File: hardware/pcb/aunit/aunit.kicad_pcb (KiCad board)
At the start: 2 copper layers, 62.2 x 21.6 mm, 48 parts, among them J1 BUS, J2 Input A, J3 Input B, J4 Control, J5 Flags, J6 Power, U1 74HC283, U2 74HC283, U3 74HC86, U4 74HC86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

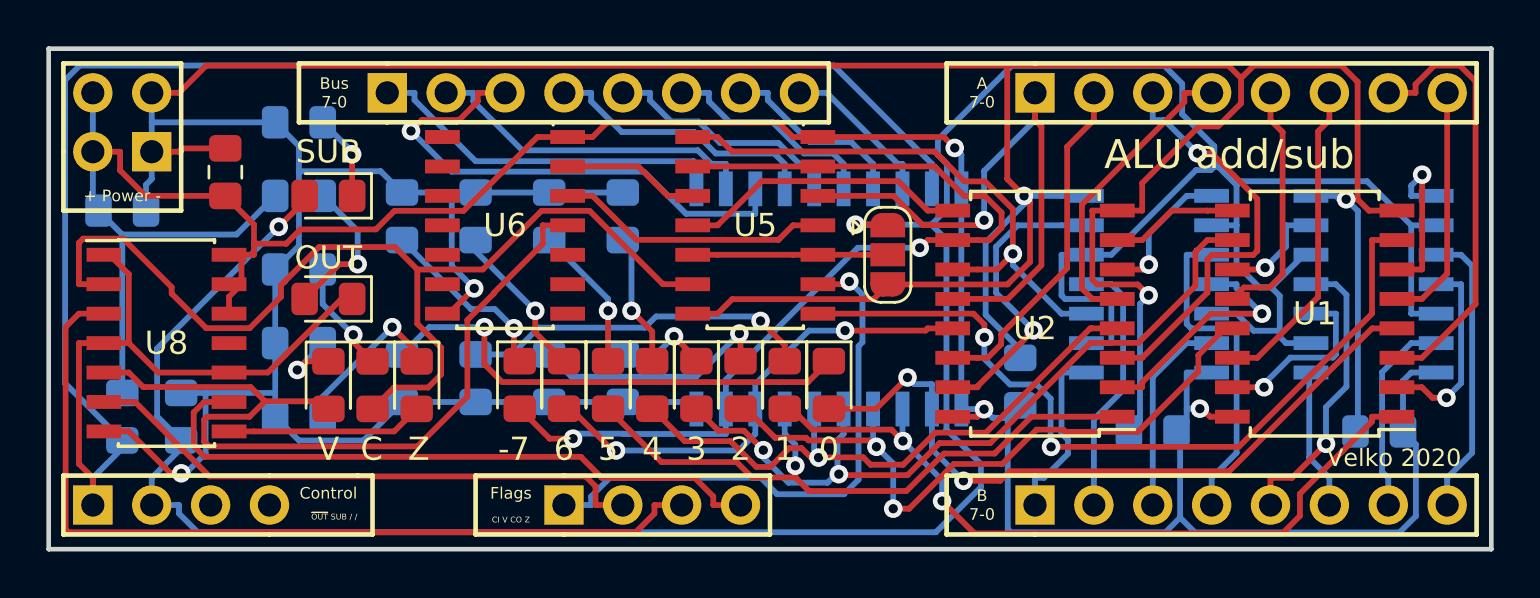
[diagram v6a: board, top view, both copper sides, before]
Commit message: Re-connect unused gate inputs, move input capacitor
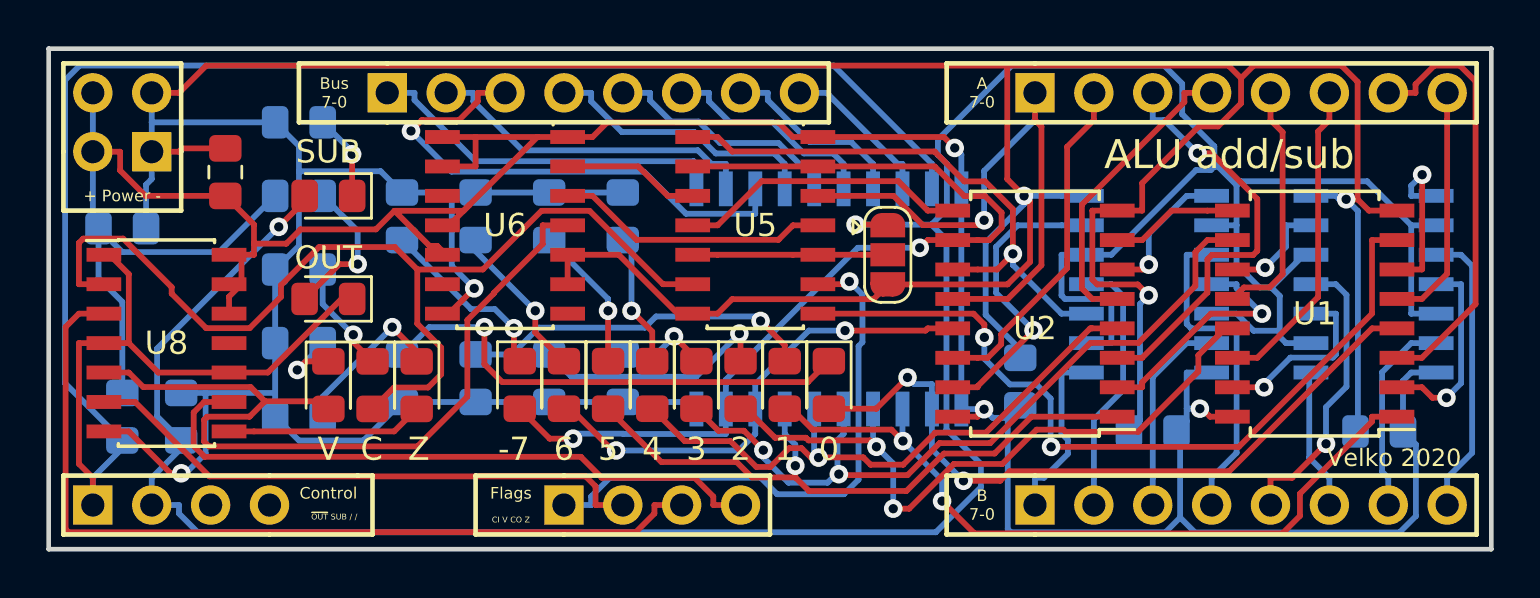
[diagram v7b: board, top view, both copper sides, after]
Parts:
- moved C1 0.76 mm to (38.1, 43.9)
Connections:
- U6 pad 1: Net-(U6-Pad1) -> VCC
- U6 pad 10: Net-(U6-Pad10) -> GND
- U6 pad 2: Net-(U6-Pad2) -> VCC
- U6 pad 4: Net-(U6-Pad4) -> VCC
- U6 pad 5: Net-(U6-Pad5) -> VCC
- U6 pad 9: Net-(U6-Pad9) -> GND
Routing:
- net VCC: track 124.4 -> 137.5 mm
- net GND: track 209.5 -> 217.9 mm
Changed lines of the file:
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@@
     (thickness 1.6)
     (drawings 52)
-    (tracks 846)
+    (tracks 862)
     (zones 0)
     (modules 48)
-    (nets 83)
+    (nets 77)
   )
   (page A4)
@@
   (net 75 "Net-(U6-Pad6)")
   (net 76 "Net-(U6-Pad8)")
-  (net 77 "Net-(U6-Pad10)")
-  (net 78 "Net-(U6-Pad9)")
-  (net 79 "Net-(U6-Pad5)")
-  (net 80 "Net-(U6-Pad4)")
-  (net 81 "Net-(U6-Pad2)")
-  (net 82 "Net-(U6-Pad1)")
   (net_class Default "This is the default net class."
     (clearance 0.2)
@@
     (add_net "Net-(U5-Pad11)")
     (add_net "Net-(U5-Pad3)")
-    (add_net "Net-(U6-Pad1)")
-    (add_net "Net-(U6-Pad10)")
-    (add_net "Net-(U6-Pad2)")
     (add_net "Net-(U6-Pad3)")
-    (add_net "Net-(U6-Pad4)")
-    (add_net "Net-(U6-Pad5)")
     (add_net "Net-(U6-Pad6)")
     (add_net "Net-(U6-Pad8)")
-    (add_net "Net-(U6-Pad9)")
     (add_net "Net-(U8-Pad11)")
     (add_net OOUT)
@@
   )
   (module Capacitor_SMD:C_0805_2012Metric_Pad1.15x1.40mm_HandSolder (layer B.Cu)
-    (at 38.1 43.18)
+    (at 38.1 43.942)
     (descr "Capacitor SMD 0805 (2012 Metric), square (rectangular) end terminal, IPC_7351 nominal with elongated pad for handsoldering. (Body size source: https://docs.google.com/spreadsheets/d/1BsfQQcO9C6DZCsRaXUlFlo91Tg2WpOkGARC1WS5S8t0/edit?usp=sharing), generated with kicad-footprint-generator")
     (tags "capacitor handsolder")
@@
       (net 20 OVFD))
     (pad 10 smd rect (at 2.7 1.27) (size 1.5 0.6) (layers F.Cu F.Paste F.Mask)
-      (net 77 "Net-(U6-Pad10)"))
+      (net 2 GND))
     (pad 9 smd rect (at 2.7 2.54) (size 1.5 0.6) (layers F.Cu F.Paste F.Mask)
-      (net 78 "Net-(U6-Pad9)"))
+      (net 2 GND))
     (pad 8 smd rect (at 2.7 3.81) (size 1.5 0.6) (layers F.Cu F.Paste F.Mask)
       (net 76 "Net-(U6-Pad8)"))
@@
       (net 75 "Net-(U6-Pad6)"))
     (pad 5 smd rect (at -2.7 1.27) (size 1.5 0.6) (layers F.Cu F.Paste F.Mask)
-      (net 79 "Net-(U6-Pad5)"))
+      (net 1 VCC))
     (pad 4 smd rect (at -2.7 0) (size 1.5 0.6) (layers F.Cu F.Paste F.Mask)
-      (net 80 "Net-(U6-Pad4)"))
+      (net 1 VCC))
     (pad 3 smd rect (at -2.7 -1.27) (size 1.5 0.6) (layers F.Cu F.Paste F.Mask)
       (net 61 "Net-(U6-Pad3)"))
     (pad 2 smd rect (at -2.7 -2.54) (size 1.5 0.6) (layers F.Cu F.Paste F.Mask)
-      (net 81 "Net-(U6-Pad2)"))
+      (net 1 VCC))
     (pad 1 smd rect (at -2.7 -3.81) (size 1.5 0.6) (layers F.Cu F.Paste F.Mask)
-      (net 82 "Net-(U6-Pad1)"))
+      (net 1 VCC))
     (model ${KISYS3DMOD}/Package_SO.3dshapes/SOIC-14_3.9x8.7mm_P1.27mm.wrl
       (at (xyz 0 0 0))
@@
   (segment (start 49.0406 43.99) (end 49.841 43.1896) (width 0.25) (layer F.Cu) (net 1))
   (segment (start 49.841 43.1896) (end 52.8214 43.1896) (width 0.25) (layer F.Cu) (net 1))
-  (segment (start 52.8214 43.1896) (end 56.006 40.005) (width 0.25) (layer F.Cu) (net 1))
   (segment (start 56.006 40.005) (end 57.31 40.005) (width 0.25) (layer F.Cu) (net 1))
   (segment (start 43.2427 46.355) (end 42.705 46.8927) (width 0.25) (layer F.Cu) (net 1))
@@
   (segment (start 59.0106 39.3797) (end 66.4044 39.3797) (width 0.25) (layer F.Cu) (net 1))
   (segment (start 66.4044 39.3797) (end 67.0297 40.005) (width 0.25) (layer F.Cu) (net 1))
-  (segment (start 38.1 44.2112) (end 43.0288 44.2112) (width 0.25) (layer B.Cu) (net 1))
-  (segment (start 43.0288 44.2112) (end 44.695 42.545) (width 0.25) (layer B.Cu) (net 1))
-  (segment (start 37.075 43.18) (end 37.075 43.1862) (width 0.25) (layer B.Cu) (net 1))
-  (segment (start 37.075 43.1862) (end 38.1 44.2112) (width 0.25) (layer B.Cu) (net 1))
-  (segment (start 38.1 44.2112) (end 38.1 51.045) (width 0.25) (layer B.Cu) (net 1))
-  (segment (start 36.83 40.64) (end 36.83 42.935) (width 0.25) (layer B.Cu) (net 1))
-  (segment (start 36.83 42.935) (end 37.075 43.18) (width 0.25) (layer B.Cu) (net 1))
   (segment (start 36.83 40.64) (end 38.0053 40.64) (width 0.25) (layer F.Cu) (net 1))
   (segment (start 76.2946 52.1204) (end 76.835 51.58) (width 0.25) (layer B.Cu) (net 1))
@@
   (via (at 74.0084 40.4765) (size 0.8) (layers F.Cu B.Cu) (net 1))
   (via (at 84.5819 51.7232) (size 0.8) (layers F.Cu B.Cu) (net 1))
+  (segment (start 51.91 41.275) (end 53.34 41.275) (width 0.25) (layer F.Cu) (net 1))
+  (segment (start 53.34 41.275) (end 53.34 40.005) (width 0.25) (layer F.Cu) (net 1))
+  (segment (start 51.91 40.005) (end 53.34 40.005) (width 0.25) (layer F.Cu) (net 1))
+  (segment (start 53.34 40.005) (end 56.006 40.005) (width 0.25) (layer F.Cu) (net 1))
+  (segment (start 53.0855 42.9255) (end 52.196 43.815) (width 0.25) (layer F.Cu) (net 1))
+  (segment (start 53.0855 42.9255) (end 56.006 40.005) (width 0.25) (layer F.Cu) (net 1))
+  (segment (start 52.196 43.815) (end 51.91 43.815) (width 0.25) (layer F.Cu) (net 1))
+  (segment (start 52.8214 43.1896) (end 53.0855 42.9255) (width 0.25) (layer F.Cu) (net 1))
+  (segment (start 51.91 45.085) (end 51.91 44.925) (width 0.25) (layer F.Cu) (net 1))
+  (segment (start 51.3554 44.704) (end 49.841 43.1896) (width 0.25) (layer F.Cu) (net 1))
+  (segment (start 51.689 44.704) (end 51.3554 44.704) (width 0.25) (layer F.Cu) (net 1))
+  (segment (start 51.91 44.925) (end 51.689 44.704) (width 0.25) (layer F.Cu) (net 1))
+  (segment (start 36.83 43.697) (end 37.075 43.942) (width 0.25) (layer B.Cu) (net 1))
+  (segment (start 36.83 40.64) (end 36.83 43.697) (width 0.25) (layer B.Cu) (net 1))
+  (segment (start 44.695 42.545) (end 42.27299 44.96701) (width 0.25) (layer B.Cu) (net 1))
+  (segment (start 38.1 51.045) (end 38.1 47.117) (width 0.25) (layer B.Cu) (net 1))
+  (segment (start 37.075 46.092) (end 37.075 43.942) (width 0.25) (layer B.Cu) (net 1))
+  (segment (start 38.1 47.117) (end 37.075 46.092) (width 0.25) (layer B.Cu) (net 1))
+  (segment (start 38.10001 44.96701) (end 37.075 43.942) (width 0.25) (layer B.Cu) (net 1))
+  (segment (start 42.27299 44.96701) (end 38.10001 44.96701) (width 0.25) (layer B.Cu) (net 1))
   (segment (start 52.3131 42.4) (end 50.165 42.4) (width 0.25) (layer B.Cu) (net 2))
   (segment (start 53.34 42.4) (end 52.3131 42.4) (width 0.25) (layer B.Cu) (net 2))
@@
   (segment (start 39.37 40.64) (end 39.37 41.8153) (width 0.25) (layer B.Cu) (net 2))
   (segment (start 39.37 41.8153) (end 39.125 42.0603) (width 0.25) (layer B.Cu) (net 2))
-  (segment (start 39.125 42.0603) (end 39.125 43.18) (width 0.25) (layer B.Cu) (net 2))
   (segment (start 39.37 39.37) (end 39.37 40.64) (width 0.25) (layer B.Cu) (net 2))
   (segment (start 76.9991 42.545) (end 78.6147 42.545) (width 0.25) (layer B.Cu) (net 2))
@@
   (via (at 90.8934 42.6926) (size 0.8) (layers F.Cu B.Cu) (net 2))
   (via (at 76.9991 42.545) (size 0.8) (layers F.Cu B.Cu) (net 2))
+  (segment (start 57.31 45.085) (end 57.31 46.355) (width 0.25) (layer F.Cu) (net 2))
+  (segment (start 62.05609 47.625) (end 62.705 47.625) (width 0.25) (layer F.Cu) (net 2))
+  (segment (start 59.51609 45.085) (end 62.05609 47.625) (width 0.25) (layer F.Cu) (net 2))
+  (segment (start 57.31 45.085) (end 59.51609 45.085) (width 0.25) (layer F.Cu) (net 2))
+  (segment (start 39.125 42.0603) (end 39.125 43.942) (width 0.25) (layer B.Cu) (net 2))
   (segment (start 68.58 49.675) (end 67.6786 50.5764) (width 0.25) (layer F.Cu) (net 3))
   (segment (start 67.6786 50.5764) (end 54.4907 50.5764) (width 0.25) (layer F.Cu) (net 3))
